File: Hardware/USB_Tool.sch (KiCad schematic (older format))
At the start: 41 parts, among them J1 USB_B_Micro, J2 CONN_ICSP, J3 Extender_I2C_1, J4 Extender_I2C_2, J5 Extender_I2C_3, P1 TLMS1000, P2 150141M173100, SW1 SW_2TO1, U1 MRF89XAM8A, U2 NCP114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

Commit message: Issues fix
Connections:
- net 5V: no longer R2.1
- net CS_EXT: now also U4.36 (RC2); no longer U4.27 (RE2)
- net DAC1: no longer U4.21 (RA2)
- net IRQ0: now also U4.32 (RC0); no longer U4.25 (RE0)
- net IRQ1: now also U4.35 (RC1); no longer U4.26 (RE1)
- net VCC: now also R2.1
- net LED_0 renamed LED_B
- net LED_B: now also U4.25 (RE0); no longer U4.32 (RC0)
- net LED_1 renamed LED_G
- net LED_G: now also U4.26 (RE1); no longer U4.35 (RC1)
- net LED_2 renamed LED_R
- net LED_R: now also U4.27 (RE2); no longer U4.36 (RC2)
- new net INT: U4.21 (RA2)
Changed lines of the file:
@@
 	1    0    0    -1
 $EndComp
-Wire Wire Line
-	7550 3650 7150 3650
 $Comp
 L 0EsseivaN_Lib:CONN_01X08 X2
@@
 Text Label 10600 3750 2    50   ~ 0
 5V
-Wire Wire Line
-	7150 3750 7600 3750
-Wire Wire Line
-	7600 3750 7600 2500
-Wire Wire Line
-	7600 2500 8000 2500
-Wire Wire Line
-	8000 2500 8000 2400
-Wire Wire Line
-	7150 3850 7650 3850
-Wire Wire Line
-	7650 3850 7650 2550
-Wire Wire Line
-	7650 2550 8250 2550
-Wire Wire Line
-	8250 2550 8250 2400
-Text Label 7200 3650 0    50   ~ 0
-LED_0
-Text Label 7200 3750 0    50   ~ 0
-LED_1
-Text Label 7200 3850 0    50   ~ 0
-LED_2
 Text Label 10600 3950 2    50   ~ 0
 DAC1
@@
 Text Label 9400 3600 2    50   ~ 0
 GND
-Text Label 7200 5450 0    50   ~ 0
+Text Label 7200 3650 0    50   ~ 0
 IRQ0
-Text Label 7200 5550 0    50   ~ 0
+Text Label 7200 3750 0    50   ~ 0
 IRQ1
-Text Label 7200 5650 0    50   ~ 0
+Text Label 7200 3850 0    50   ~ 0
 CS_EXT
 Text Label 3800 5350 0    50   ~ 0
@@
 Connection ~ 4600 6700
 Entry Wire Line
-	7550 5450 7650 5550
-Entry Wire Line
-	7550 5550 7650 5650
-Entry Wire Line
-	7550 5650 7650 5750
-Wire Wire Line
-	7550 5550 7150 5550
-Wire Wire Line
-	7150 5450 7550 5450
-Wire Wire Line
-	7550 5650 7150 5650
+	7550 3650 7650 3550
+Entry Wire Line
+	7550 3750 7650 3650
+Entry Wire Line
+	7550 3850 7650 3750
+Wire Wire Line
+	7550 3750 7150 3750
+Wire Wire Line
+	7150 3650 7550 3650
+Wire Wire Line
+	7550 3850 7150 3850
 Wire Bus Line
 	5300 2800 7800 2800
@@
 	5200 3850 5550 3850
 Text Label 5500 3850 2    50   ~ 0
-DAC1
+INT
 Text Label 5500 4250 2    50   ~ 0
 CLK
@@
 Wire Wire Line
 	7700 4050 7150 4050
-Wire Wire Line
-	7150 3950 7700 3950
 Entry Wire Line
 	7700 3950 7800 3850
@@
 $EndComp
 Wire Wire Line
-	7550 2450 7750 2450
-Wire Wire Line
-	7750 2450 7750 2400
-Wire Wire Line
-	7550 2450 7550 3650
-Wire Wire Line
 	7750 2000 7750 1900
 Wire Wire Line
@@
 $EndComp
 $Comp
-L 0EsseivaN_Lib:5V #PWR0116
-U 1 1 5CBEEF46
-P 2150 2300
-F 0 "#PWR0116" H 2150 2150 50  0001 C CNN
-F 1 "5V" H 2097 2337 45  0000 R CNN
-F 2 "" H 2150 2300 50  0000 C CNN
-F 3 "" H 2150 2300 50  0000 C CNN
-	1    2150 2300
-	1    0    0    -1
-$EndComp
-$Comp
 L 0EsseivaN_Lib:VCC #PWR0122
 U 1 1 5CDA9820
@@
 Wire Wire Line
 	6350 1050 6000 1050
+Connection ~ 6000 1050
+Wire Wire Line
+	7150 3950 7700 3950
+Text Label 7200 5450 0    50   ~ 0
+LED_B
+Text Label 7200 5550 0    50   ~ 0
+LED_G
+Text Label 7200 5650 0    50   ~ 0
+LED_R
+Wire Wire Line
+	7150 5450 8150 5450
+Wire Wire Line
+	8150 5450 8150 2700
+Wire Wire Line
+	8150 2700 7750 2700
+Wire Wire Line
+	7150 5550 8200 5550
+Wire Wire Line
+	8200 5550 8200 2650
+Wire Wire Line
+	8200 2650 8000 2650
+Wire Wire Line
+	7150 5650 8250 5650
+Wire Wire Line
+	8250 2400 8250 5650
+Wire Wire Line
+	8000 2400 8000 2650
+Wire Wire Line
+	7750 2400 7750 2700
 Wire Bus Line
 	1850 4500 4200 4500
@@
 	1200 5950 1200 6700
 Wire Bus Line
-	7650 5550 7650 6350
+	7650 3550 7650 6350
 Wire Bus Line
 	5000 3450 5300 3450
@@
 Wire Bus Line
 	4600 4250 4600 6700
-Connection ~ 6000 1050
+$Comp
+L 0EsseivaN_Lib:VCC #PWR?
+U 1 1 5D080FD6
+P 2150 2300
+F 0 "#PWR?" H 2150 2150 50  0001 C CNN
+F 1 "VCC" H 2097 2337 50  0000 R CNN
+F 2 "" H 2150 2300 50  0000 C CNN
+F 3 "" H 2150 2300 50  0000 C CNN
+	1    2150 2300
+	1    0    0    -1
+$EndComp
 $EndSCHEMATC

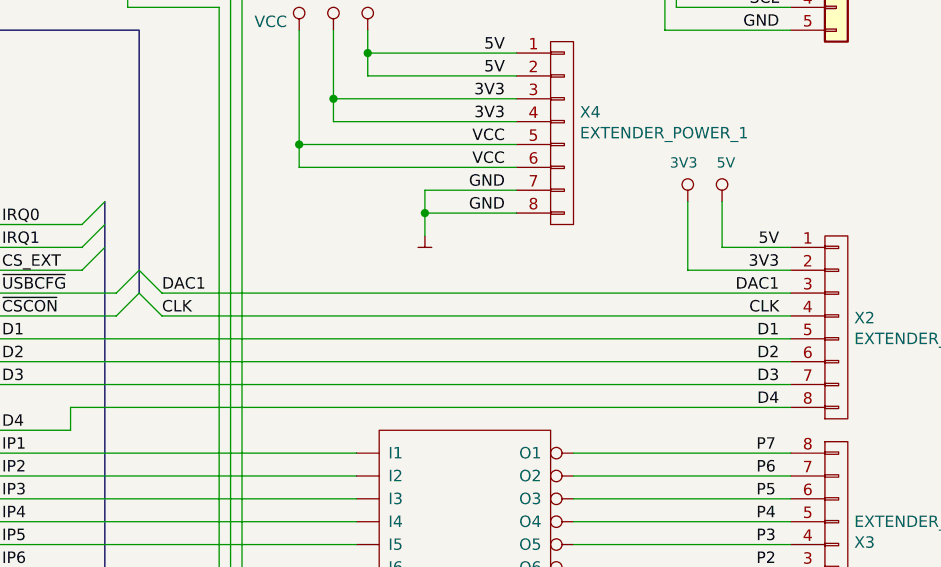
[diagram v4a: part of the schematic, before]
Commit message: v2
Changed led from PORTB to PORTE
Changed IRQ0,1 & CS_EXIT to PORTB for IOC
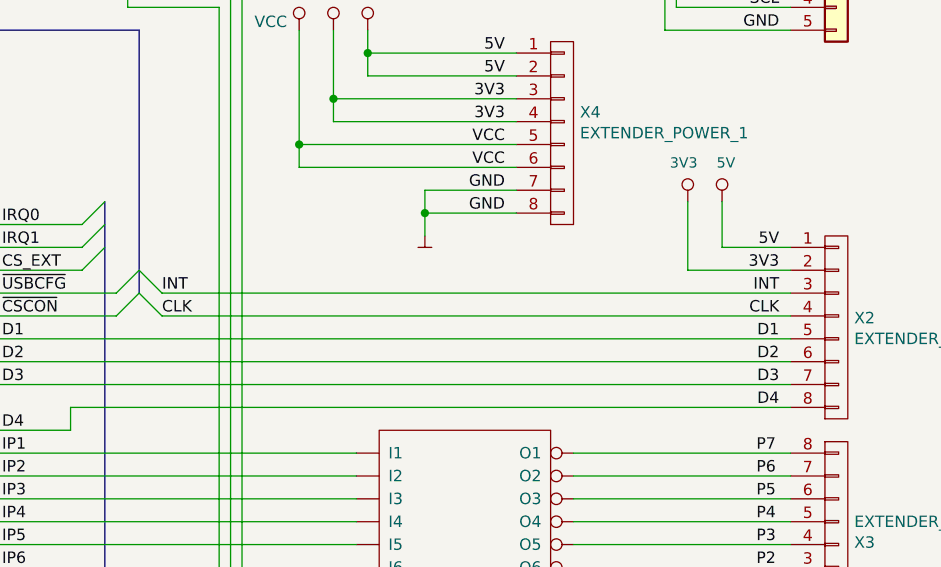
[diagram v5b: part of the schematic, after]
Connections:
- net DAC1 is gone; now on net INT: X2.3 (P3)
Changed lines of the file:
@@
 5V
 Text Label 10600 3950 2    50   ~ 0
-DAC1
+INT
 Text Label 10600 4050 2    50   ~ 0
 CLK
@@
 CLK
 Text Label 7900 3950 0    50   ~ 0
-DAC1
+INT
 $Comp
 L 0EsseivaN_Lib:CONN_01X02 X5
@@
 Wire Wire Line
 	7750 2400 7750 2700
-Wire Bus Line
-	1850 4500 4200 4500
-Wire Bus Line
-	7800 2800 7800 3950
-Wire Bus Line
-	1200 5950 1200 6700
-Wire Bus Line
-	7650 3550 7650 6350
-Wire Bus Line
-	5000 3450 5300 3450
-Wire Bus Line
-	3950 3700 3950 4250
-Wire Bus Line
-	1850 3100 1850 4500
-Wire Bus Line
-	4200 3500 4200 4500
-Wire Bus Line
-	4600 4250 4600 6700
-$Comp
-L 0EsseivaN_Lib:VCC #PWR?
+$Comp
+L 0EsseivaN_Lib:VCC #PWR0116
 U 1 1 5D080FD6
 P 2150 2300
-F 0 "#PWR?" H 2150 2150 50  0001 C CNN
+F 0 "#PWR0116" H 2150 2150 50  0001 C CNN
 F 1 "VCC" H 2097 2337 50  0000 R CNN
 F 2 "" H 2150 2300 50  0000 C CNN
@@
 	1    0    0    -1
 $EndComp
+Wire Bus Line
+	1850 4500 4200 4500
+Wire Bus Line
+	7800 2800 7800 3950
+Wire Bus Line
+	1200 5950 1200 6700
+Wire Bus Line
+	7650 3550 7650 6350
+Wire Bus Line
+	5000 3450 5300 3450
+Wire Bus Line
+	3950 3700 3950 4250
+Wire Bus Line
+	1850 3100 1850 4500
+Wire Bus Line
+	4200 3500 4200 4500
+Wire Bus Line
+	4600 4250 4600 6700
 $EndSCHEMATC

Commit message: Some fix
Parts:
- removed C9: 100nF, 0EsseivaN_Lib:C_1206_HandSoldering, symbol 0EsseivaN_Lib:CAPA
- removed U5: ULN2003, 0EsseivaN_Lib:SOIC-16_3.9x9.9mm_Pitch1.27mm, symbol 0EsseivaN_Lib:ULN200x
- removed X2: EXTENDER_IO_1, 0EsseivaN_Lib:CH_08P, symbol 0EsseivaN_Lib:CONN_01X08
- removed X4: EXTENDER_POWER_1, 0EsseivaN_Lib:CH_08P, symbol 0EsseivaN_Lib:CONN_01X08
- removed X5: EXTENDER_COM, 0EsseivaN_Lib:CH_02P, symbol 0EsseivaN_Lib:CONN_01X02
- added R12, R13: 1k, 0EsseivaN_Lib:R_0603_HandSoldering, symbol 0EsseivaN_Lib:R
- added X2: EXTENDER_IO_1, 0EsseivaN_Lib:CH_05P, symbol 0EsseivaN_Lib:CONN_01X05
- added X4, X5: EXTENDER_POWER_2, 0EsseivaN_Lib:CH_04P, symbol 0EsseivaN_Lib:CONN_01X04
- X1: footprint 0EsseivaN_Lib:CH_07P -> 0EsseivaN_Lib:CH_04P; symbol 0EsseivaN_Lib:CONN_01X07 -> 0EsseivaN_Lib:CONN_01X04
- X7: renamed from J3; footprint 0EsseivaN_Lib:CH_05P -> 0EsseivaN_Lib:CH_02P; symbol Connector_Generic:Conn_01x05 -> 0EsseivaN_Lib:CONN_01X02
- X8: renamed from J4; footprint 0EsseivaN_Lib:CH_05P -> 0EsseivaN_Lib:CH_02P; symbol Connector_Generic:Conn_01x05 -> 0EsseivaN_Lib:CONN_01X02
- X9: renamed from J5; footprint 0EsseivaN_Lib:CH_05P -> 0EsseivaN_Lib:CH_02P; symbol Connector_Generic:Conn_01x05 -> 0EsseivaN_Lib:CONN_01X02
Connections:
- net P1 is gone; now on net D10: X3.2 (P2)
- net P2 is gone; now on net D9: X3.3 (P3)
- net P3 is gone; now on net D8: X3.4 (P4)
- net P4 is gone; now on net D7: X3.5 (P5)
- net P5 is gone; now on net D6: X3.6 (P6)
- net P6 is gone; now on net D5: X3.7 (P7)
- net P7 is gone; now on net D4: X3.8 (P8)
- net 3V3: now also X4.2 (P2), X5.2 (P2); no longer X1.2 (P2), X7.2 (Pin_2), X8.2 (Pin_2), X9.2 (Pin_2)
- net 5V: now also P2.1 (Anode), R12.2, R13.2, X4.1 (P1), X5.1 (P1); no longer X1.1 (P1), X7.1 (Pin_1), X8.1 (Pin_1), X9.1 (Pin_1)
- net CLK: now also X2.2 (P2)
- net CS_EXT: now also X1.4 (P4); no longer X1.6 (P6)
- net D1: now also X2.3 (P3)
- net D2: now also X2.4 (P4)
- net D3: now also X2.5 (P5)
- net GND: now also X4.4 (P4), X5.4 (P4); no longer X1.7 (P7), X3.1 (P1), X7.5 (Pin_5), X8.5 (Pin_5), X9.5 (Pin_5)
- net INT: now also X2.1 (P1)
- net MISO: now also X1.3 (P3); no longer X1.5 (P5)
- net MOSI: now also X1.2 (P2); no longer X1.4 (P4)
- net SCK: now also X1.1 (P1); no longer X1.3 (P3)
- net SCL: now also X7.2 (P2), X8.2 (P2), X9.2 (P2), R13.1; no longer X7.4 (Pin_4), X8.4 (Pin_4), X9.4 (Pin_4)
- net SDA: now also X7.1 (P1), X8.1 (P1), X9.1 (P1), R12.1; no longer X7.3 (Pin_3), X8.3 (Pin_3), X9.3 (Pin_3)
- net VCC: now also X4.3 (P3), X5.3 (P3)
- net IP1 renamed D5
- net IP2 renamed D6
- net IP3 renamed D7
- net IP4 renamed D8
- net IP5 renamed D9
- net IP6 renamed D10
- net IP7 renamed D11
- net D11: now also X3.1 (P1)
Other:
- note removed: "WARNING : Power MCP2210 and\nPIC with same voltages"
- moved on the sheet: P2, R6, R7, R8, X3

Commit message: v4
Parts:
- removed X6: MCU_POWER_SELECT, 0EsseivaN_Lib:Pin_Header_Straight_1x03_Pitch2.54mm, symbol 0EsseivaN_Lib:CONN_01X03
- added C9: 100nF, 0EsseivaN_Lib:C_1206_HandSoldering, symbol 0EsseivaN_Lib:CAPA
- added P3, P4: Green, 0EsseivaN_Lib:D_0603_HandSoldering, symbol 0EsseivaN_Lib:LED
- added R14: 270R, 0EsseivaN_Lib:R_0603_HandSoldering, symbol 0EsseivaN_Lib:R
- added R15: 120R, 0EsseivaN_Lib:R_0603_HandSoldering, symbol 0EsseivaN_Lib:R
- C2: footprint 0EsseivaN_Lib:CP_Radial_D5.0mm_P2.00mm -> 0EsseivaN_Lib:C_0805_HandSoldering
- F1: footprint 0EsseivaN_Lib:Fuse_SMD1206_HandSoldering -> 0EsseivaN_Lib:Fuse_SMD2410_HandSoldering
- R2: value 180R -> 150R
- R4: value 1k -> 10k
- X4, X5: footprint 0EsseivaN_Lib:CH_04P -> 0EsseivaN_Lib:CH_03P; symbol 0EsseivaN_Lib:CONN_01X04 -> 0EsseivaN_Lib:CONN_01X03
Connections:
- net 3V3: now also C4.1, C5.2, C8.1, R12.2, R13.2, R2.1, R4.2, U3.1 (Vdd), U3.17 (VUSB), U4.28 (VDD), U4.7 (VDD), R15.1
- net 5V: now also R14.1; no longer R12.2, R13.2
- net GND: now also X4.3 (P3), X5.3 (P3), C9.2, P3.2 (Cathode), P4.2 (Cathode); no longer X4.4 (P4), X5.4 (P4)
- net RESET_USB: now also C9.1
- removed net VCC: C5.2, C8.1, R2.1, R4.2, U3.1 (Vdd), U4.28 (VDD), U4.7 (VDD), X4.3 (P3), X5.3 (P3)
- new net: P3.1 (Anode), R14.2
- new net: P4.1 (Anode), R15.2
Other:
- note added: "3V3 MAX !"
- note removed: "5V TO 3V3 LDO"
- moved on the sheet: C3, R12, R13, R3, R4, R5, X7, X8, X9, Y1
